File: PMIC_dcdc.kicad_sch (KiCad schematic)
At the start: 1 part, among them U3 RK809

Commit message: PMIC DCDC
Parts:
- added C10, C15, C16: 10uF X5R 6.3V, Resistor_SMD:R_0603_1608Metric, symbol Device:C
- added C11, C12, C13, C14, C17: 22uF X5R 6.3V, Resistor_SMD:R_0603_1608Metric, symbol Device:C
- added C18: 10uF 10V X5R, Capacitor_SMD:C_0201_0603Metric, symbol Device:C
- added C19: 10uF 10V X5R 10V, Capacitor_SMD:C_0201_0603Metric, symbol Device:C
- added C20: 22uF X5R 6.3V, Capacitor_SMD:C_0201_0603Metric, symbol Device:C
- added C9: 10uF 10V X5R, symbol Device:C
- added L1, L2, L3, L4: 470nH 0.035ohm, symbol Device:L
- added R11, R12: 100R 5%, Resistor_SMD:R_0402_1005Metric, symbol Device:R
- added R13: 110K 1%, Resistor_SMD:R_0402_1005Metric, symbol Device:R
- added R14: 120K 1%, Resistor_SMD:R_0402_1005Metric, symbol Device:R
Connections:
- net VCC5V0_SYS: now reaches U3.10 (VCC2)
- net VCC5V0_SYS: now also U3.11 (VCC1), U3.24 (VCC3), U3.66 (VCC4), C18.2, C19.2, C9.2
- net at U3.12 (SW1): now also L1.2
- net VDD_NPU_VEPU: now reaches U3.13 (FB1)
- net VDD_NPU_VEPU: now also C10.1, C11.1, C12.1, L1.1, R11.1, R11.2
- net at U3.25 (SW3): now also L3.2
- net VDD_DDR: now reaches U3.26 (VBUCK3)
- net VDD_DDR: now also C16.1, C17.1, L3.1, R13.1
- net at U3.27 (FB3): now also R13.2, R14.1
- net VCC_3V3: now reaches U3.64 (FB4)
- net VCC_3V3: now also C20.2, L4.1
- net at U3.65 (SW4): now also L4.2
- net VDD_ARM: now reaches U3.8 (FB2)
- net VDD_ARM: now also C13.1, C14.1, C15.1, L2.1, R12.1, R12.2
- net at U3.9 (SW2): now also L2.2
- new net GND: C10.2, C11.2, C12.2, C13.2, C14.2, C15.2, C16.2, C17.2, C18.1, C19.1, C20.1, C9.1, R14.2
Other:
- note added: "Feedback from far-end"
- company: (none) -> Qingdao IotPi Information Technology
- title: (none) -> Leaf RV1126 PMIC RK809
- moved on the sheet: U3C

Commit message: updated PMIC DCDC
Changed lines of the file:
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@@
+    (stroke (width 0) (type default))
+  )
+  (wire (pts (xy 54.61 43.18) (xy 67.31 43.18))
     (stroke (width 0) (type default))
   )
@@
     (effects (font (size 1.27 1.27)) (justify left bottom))
   )
+  (label "VCC_3V3" (at 67.31 43.18 0) (fields_autoplaced)
+    (effects (font (size 1.27 1.27)) (justify left bottom))
+  )
   (label "VCC5V0_SYS" (at 123.19 49.53 180) (fields_autoplaced)
     (effects (font (size 1.27 1.27)) (justify right bottom))
@@
     (effects (font (size 1.27 1.27)) (justify right bottom))
   )
-  (global_label "VDD_ARM" (shape input) (at 54.61 38.1 180) (fields_autoplaced)
+  (global_label "VDD_ARM" (shape output) (at 54.61 38.1 180) (fields_autoplaced)
     (effects (font (size 1.27 1.27)) (justify right))
     (property "Intersheetrefs" "${INTERSHEET_REFS}" (at 43.298 38.1 0)
@@
     )
   )
-  (global_label "VDD_DDR" (shape input) (at 54.61 33.02 180) (fields_autoplaced)
+  (global_label "VDD_DDR" (shape output) (at 54.61 33.02 180) (fields_autoplaced)
     (effects (font (size 1.27 1.27)) (justify right))
     (property "Intersheetrefs" "${INTERSHEET_REFS}" (at 43.298 33.02 0)
@@
     )
   )
-  (global_label "VDD_NPU_VEPU" (shape input) (at 54.61 27.94 180) (fields_autoplaced)
+  (global_label "VCC_3V3" (shape output) (at 54.61 43.18 180) (fields_autoplaced)
+    (effects (font (size 1.27 1.27)) (justify right))
+    (property "Intersheetrefs" "${INTERSHEET_REFS}" (at 43.6004 43.18 0)
+      (effects (font (size 1.27 1.27)) (justify right) hide)
+    )
+  )
+  (global_label "VDD_NPU_VEPU" (shape output) (at 54.61 27.94 180) (fields_autoplaced)
     (effects (font (size 1.27 1.27)) (justify right))
     (property "Intersheetrefs" "${INTERSHEET_REFS}" (at 37.3713 27.94 0)

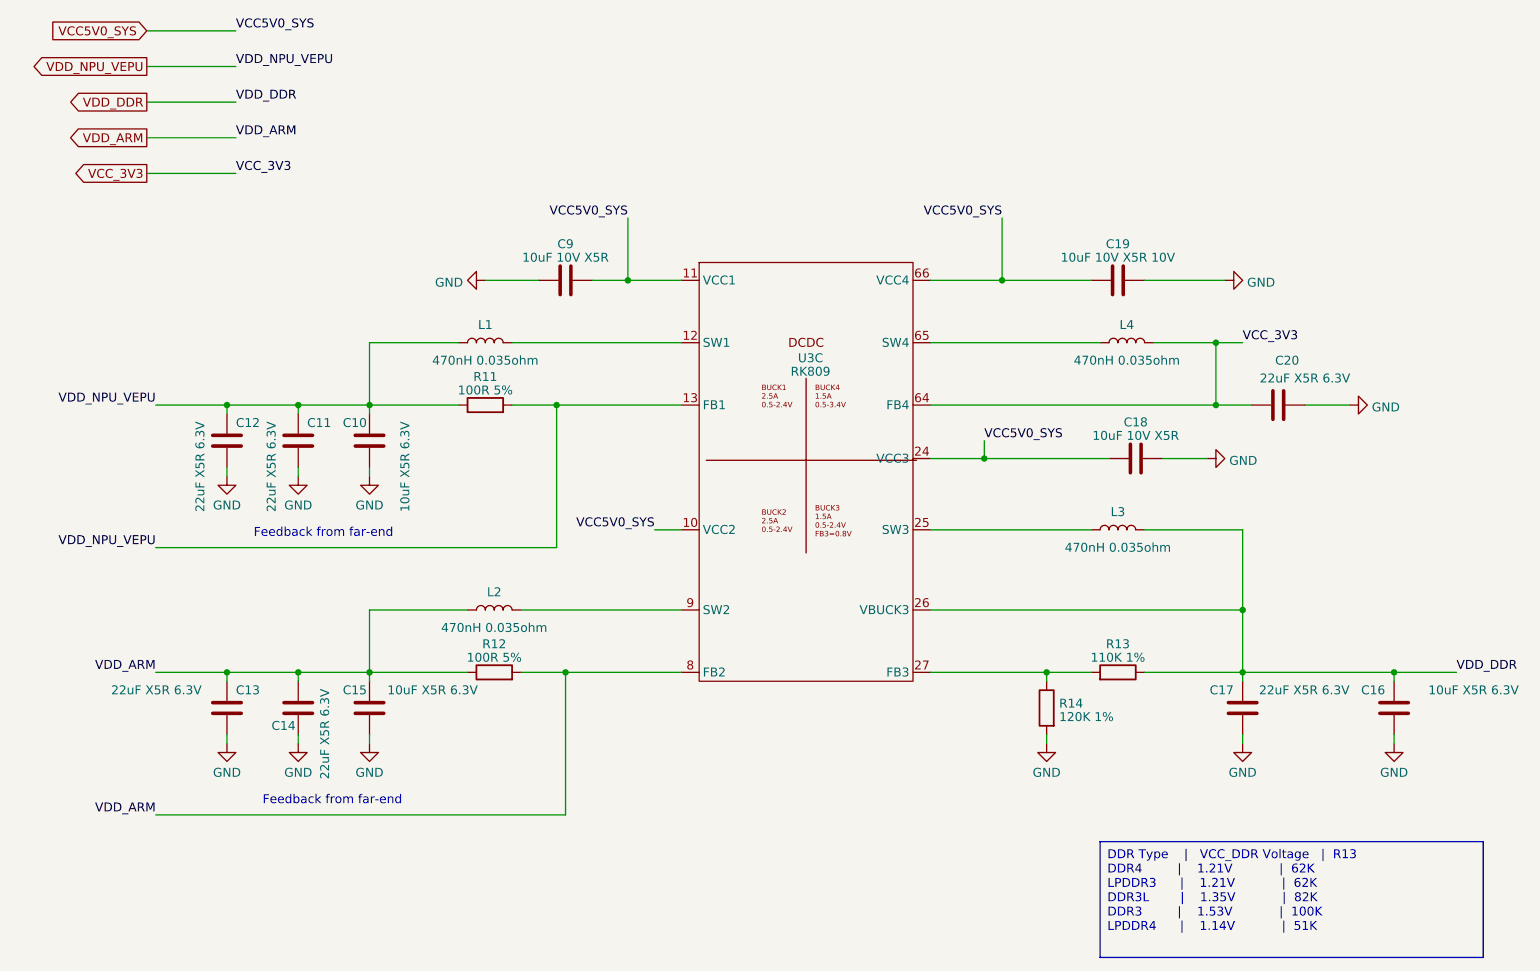
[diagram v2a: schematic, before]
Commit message: PMIC LDO
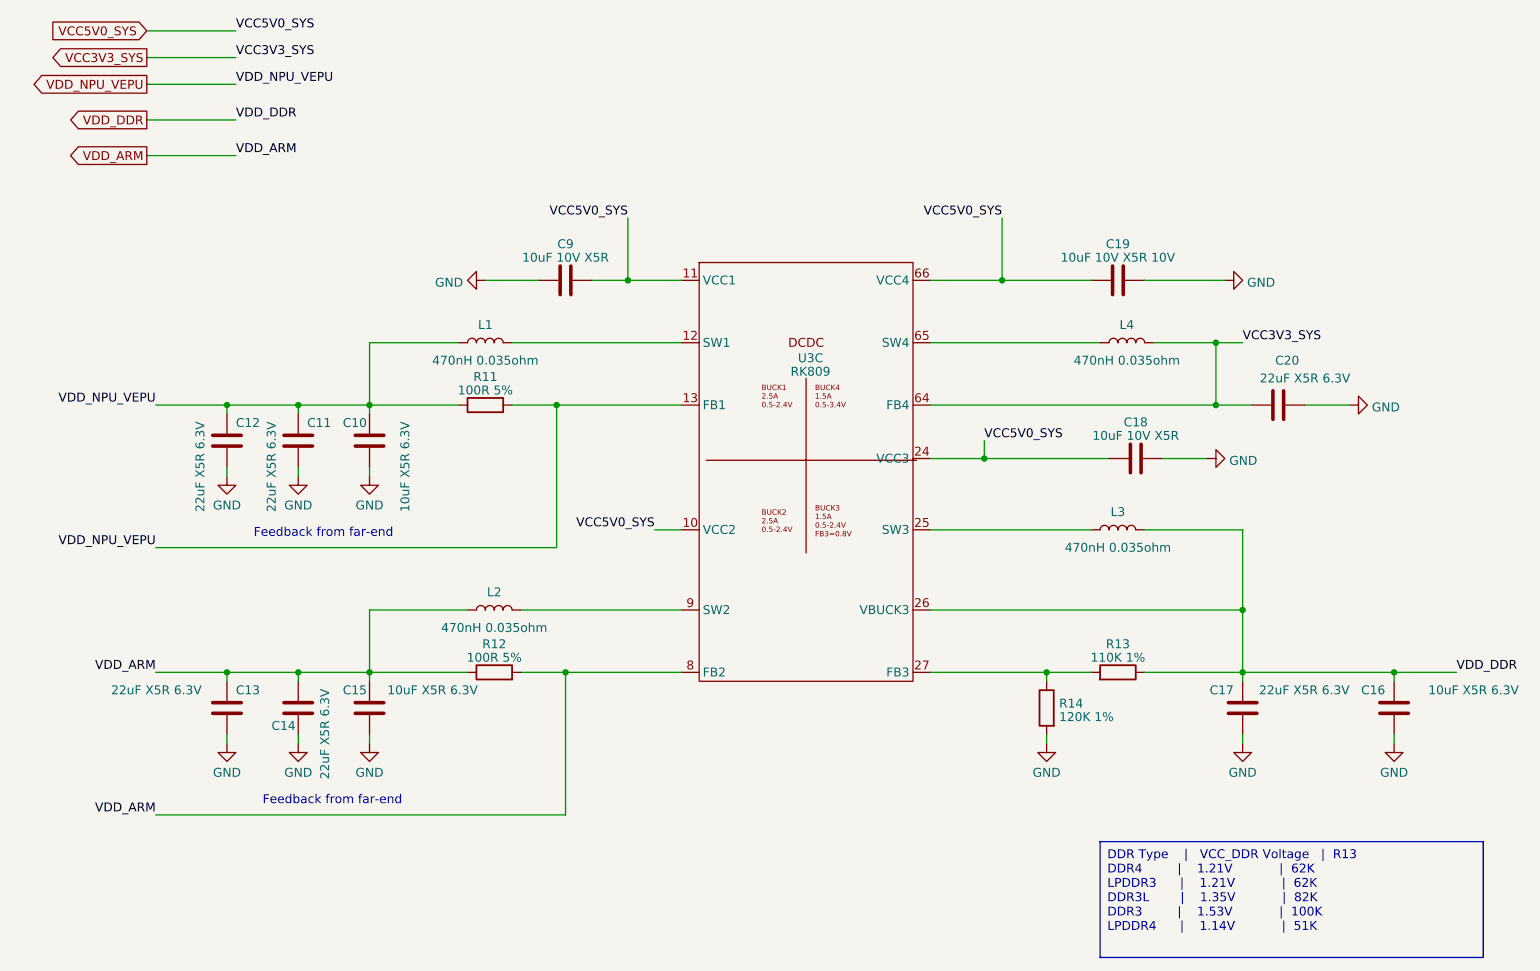
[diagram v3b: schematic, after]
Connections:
- net VCC_3V3 renamed VCC3V3_SYS
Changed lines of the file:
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@@
     (stroke (width 0) (type default))
   )
-  (wire (pts (xy 54.61 33.02) (xy 67.31 33.02))
+  (wire (pts (xy 54.61 35.56) (xy 67.31 35.56))
     (stroke (width 0) (type default))
   )
@@
     (stroke (width 0) (type default))
   )
-  (wire (pts (xy 54.61 38.1) (xy 67.31 38.1))
+  (wire (pts (xy 54.61 40.64) (xy 67.31 40.64))
     (stroke (width 0) (type default))
   )
@@
     (stroke (width 0) (type default))
   )
-  (wire (pts (xy 54.61 43.18) (xy 67.31 43.18))
+  (wire (pts (xy 54.61 26.67) (xy 67.31 26.67))
     (stroke (width 0) (type default))
   )
@@
     (stroke (width 0) (type default))
   )
-  (wire (pts (xy 54.61 27.94) (xy 67.31 27.94))
+  (wire (pts (xy 54.61 30.48) (xy 67.31 30.48))
     (stroke (width 0) (type default))
   )
@@
     (effects (font (size 1.27 1.27) (color 221 133 0 1)) (justify left bottom))
   )
-  (label "VDD_DDR" (at 67.31 33.02 0) (fields_autoplaced)
+  (label "VDD_DDR" (at 67.31 35.56 0) (fields_autoplaced)
     (effects (font (size 1.27 1.27)) (justify left bottom))
   )
@@
     (effects (font (size 1.27 1.27)) (justify left bottom))
   )
-  (label "VCC_3V3" (at 67.31 43.18 0) (fields_autoplaced)
+  (label "VCC3V3_SYS" (at 67.31 26.67 0) (fields_autoplaced)
     (effects (font (size 1.27 1.27)) (justify left bottom))
   )
@@
     (effects (font (size 1.27 1.27)) (justify right bottom))
   )
-  (label "VDD_NPU_VEPU" (at 67.31 27.94 0) (fields_autoplaced)
-    (effects (font (size 1.27 1.27)) (justify left bottom))
-  )
-  (label "VCC_3V3" (at 210.82 67.31 0) (fields_autoplaced)
+  (label "VDD_NPU_VEPU" (at 67.31 30.48 0) (fields_autoplaced)
+    (effects (font (size 1.27 1.27)) (justify left bottom))
+  )
+  (label "VCC3V3_SYS" (at 210.82 67.31 0) (fields_autoplaced)
     (effects (font (size 1.27 1.27)) (justify left bottom))
   )
@@
     (effects (font (size 1.27 1.27)) (justify right bottom))
   )
-  (label "VDD_ARM" (at 67.31 38.1 0) (fields_autoplaced)
+  (label "VDD_ARM" (at 67.31 40.64 0) (fields_autoplaced)
     (effects (font (size 1.27 1.27)) (justify left bottom))
   )
@@
     (effects (font (size 1.27 1.27)) (justify right bottom))
   )
-  (global_label "VDD_ARM" (shape output) (at 54.61 38.1 180) (fields_autoplaced)
-    (effects (font (size 1.27 1.27)) (justify right))
-    (property "Intersheetrefs" "${INTERSHEET_REFS}" (at 43.298 38.1 0)
+  (global_label "VDD_ARM" (shape output) (at 54.61 40.64 180) (fields_autoplaced)
+    (effects (font (size 1.27 1.27)) (justify right))
+    (property "Intersheetrefs" "${INTERSHEET_REFS}" (at 43.298 40.64 0)
       (effects (font (size 1.27 1.27)) (justify right) hide)
     )
@@
     )
   )
-  (global_label "VDD_DDR" (shape output) (at 54.61 33.02 180) (fields_autoplaced)
-    (effects (font (size 1.27 1.27)) (justify right))
-    (property "Intersheetrefs" "${INTERSHEET_REFS}" (at 43.298 33.02 0)
-      (effects (font (size 1.27 1.27)) (justify right) hide)
-    )
-  )
-  (global_label "VCC_3V3" (shape output) (at 54.61 43.18 180) (fields_autoplaced)
-    (effects (font (size 1.27 1.27)) (justify right))
-    (property "Intersheetrefs" "${INTERSHEET_REFS}" (at 43.6004 43.18 0)
-      (effects (font (size 1.27 1.27)) (justify right) hide)
-    )
-  )
-  (global_label "VDD_NPU_VEPU" (shape output) (at 54.61 27.94 180) (fields_autoplaced)
-    (effects (font (size 1.27 1.27)) (justify right))
-    (property "Intersheetrefs" "${INTERSHEET_REFS}" (at 37.3713 27.94 0)
-      (effects (font (size 1.27 1.27)) (justify right) hide)
-    )
+  (global_label "VDD_DDR" (shape output) (at 54.61 35.56 180) (fields_autoplaced)
+    (effects (font (size 1.27 1.27)) (justify right))
+    (property "Intersheetrefs" "${INTERSHEET_REFS}" (at 43.298 35.56 0)
+      (effects (font (size 1.27 1.27)) (justify right) hide)
+    )
+  )
+  (global_label "VCC3V3_SYS" (shape output) (at 54.61 26.67 180) (fields_autoplaced)
+    (effects (font (size 1.27 1.27)) (justify right))
+    (property "Intersheetrefs" "${INTERSHEET_REFS}" (at 40.0928 26.67 0)
+      (effects (font (size 1.27 1.27)) (justify right) hide)
+    )
+  )
+  (global_label "VDD_NPU_VEPU" (shape output) (at 54.61 30.48 180) (fields_autoplaced)
+    (effects (font (size 1.27 1.27)) (justify right))
+    (property "Intersheetrefs" "${INTERSHEET_REFS}" (at 37.3713 30.48 0)
+      (effects (font (size 1.27 1.27)) (justify right) hide)
+    )

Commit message: updated: PMIC codec
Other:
- title: Leaf RV1126 PMIC RK809 -> Leaf RV1126 PMIC RK809 Codec
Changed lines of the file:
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@@
   (paper "A4")
   (title_block
-    (title "Leaf RV1126 PMIC RK809")
-    (date "2023-02-23")
+    (title "Leaf RV1126 PMIC RK809 Codec")
+    (date "2023-02-25")
     (rev "1")
     (company "Qingdao IotPi Information Technology")

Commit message: updated: titles
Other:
- title: Leaf RV1126 PMIC RK809 Codec -> Leaf RV1126 RK809 DCDC
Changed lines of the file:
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@@
   (paper "A4")
   (title_block
-    (title "Leaf RV1126 PMIC RK809 Codec")
+    (title "Leaf RV1126 RK809 DCDC")
     (date "2023-02-25")
     (rev "1")

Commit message: Updated eMMC
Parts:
- U3: value RK809 -> RK809-2
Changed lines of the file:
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@@
       (effects (font (size 1.27 1.27)))
     )
-    (property "Value" "RK809" (at 149.225 71.4281 0)
+    (property "Value" "RK809-2" (at 149.225 71.4281 0)
       (effects (font (size 1.27 1.27)))
     )

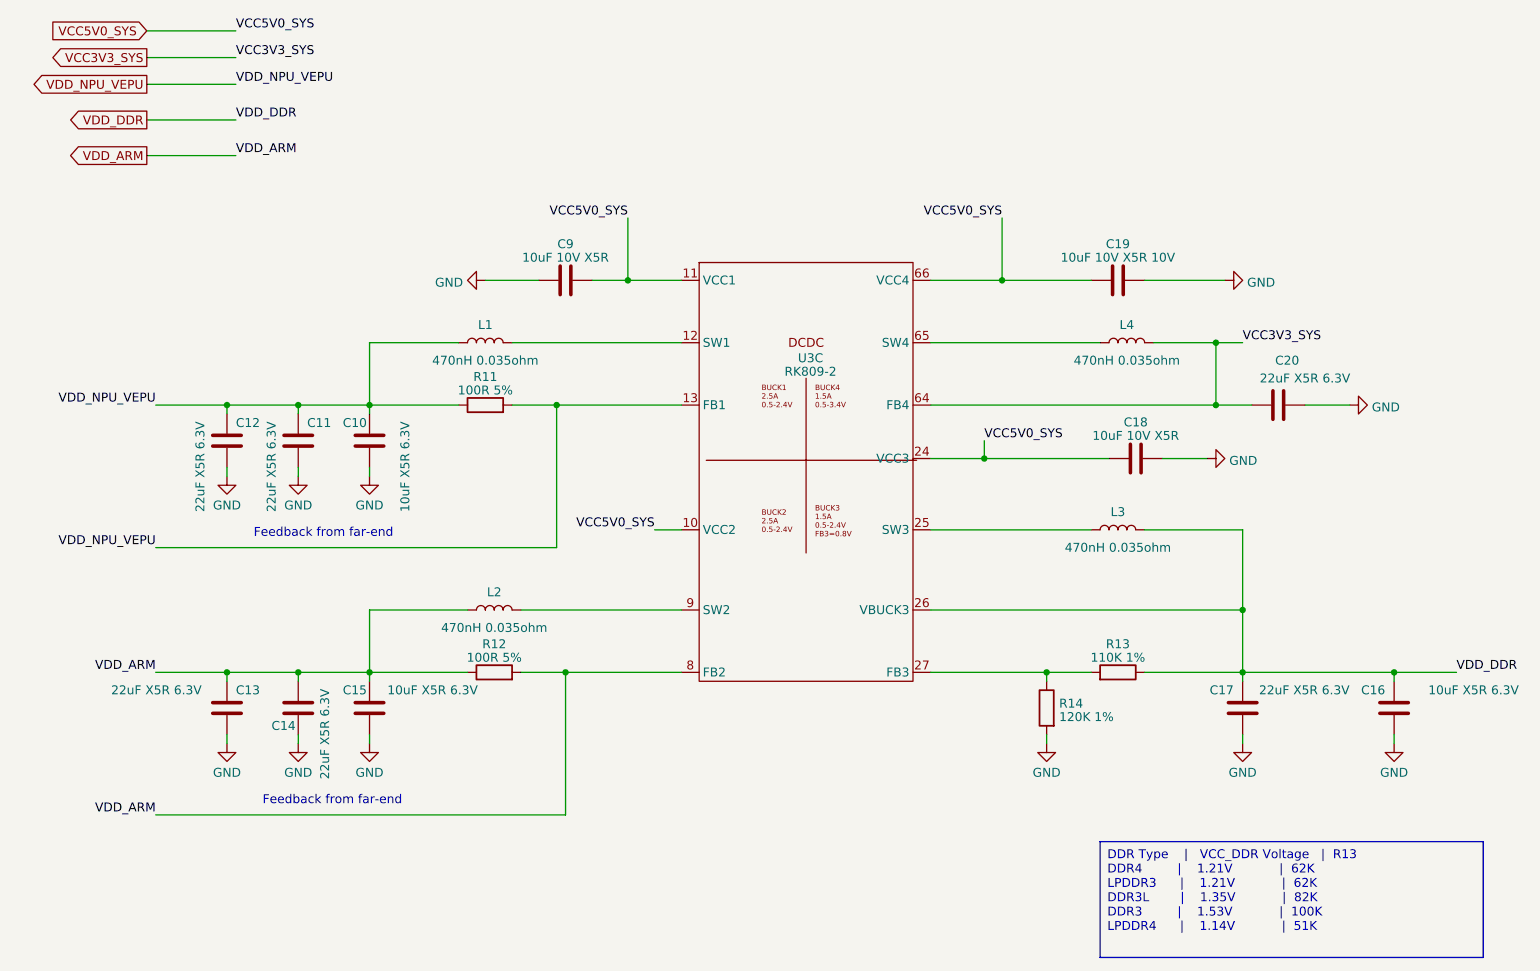
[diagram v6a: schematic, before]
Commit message: updated footprints
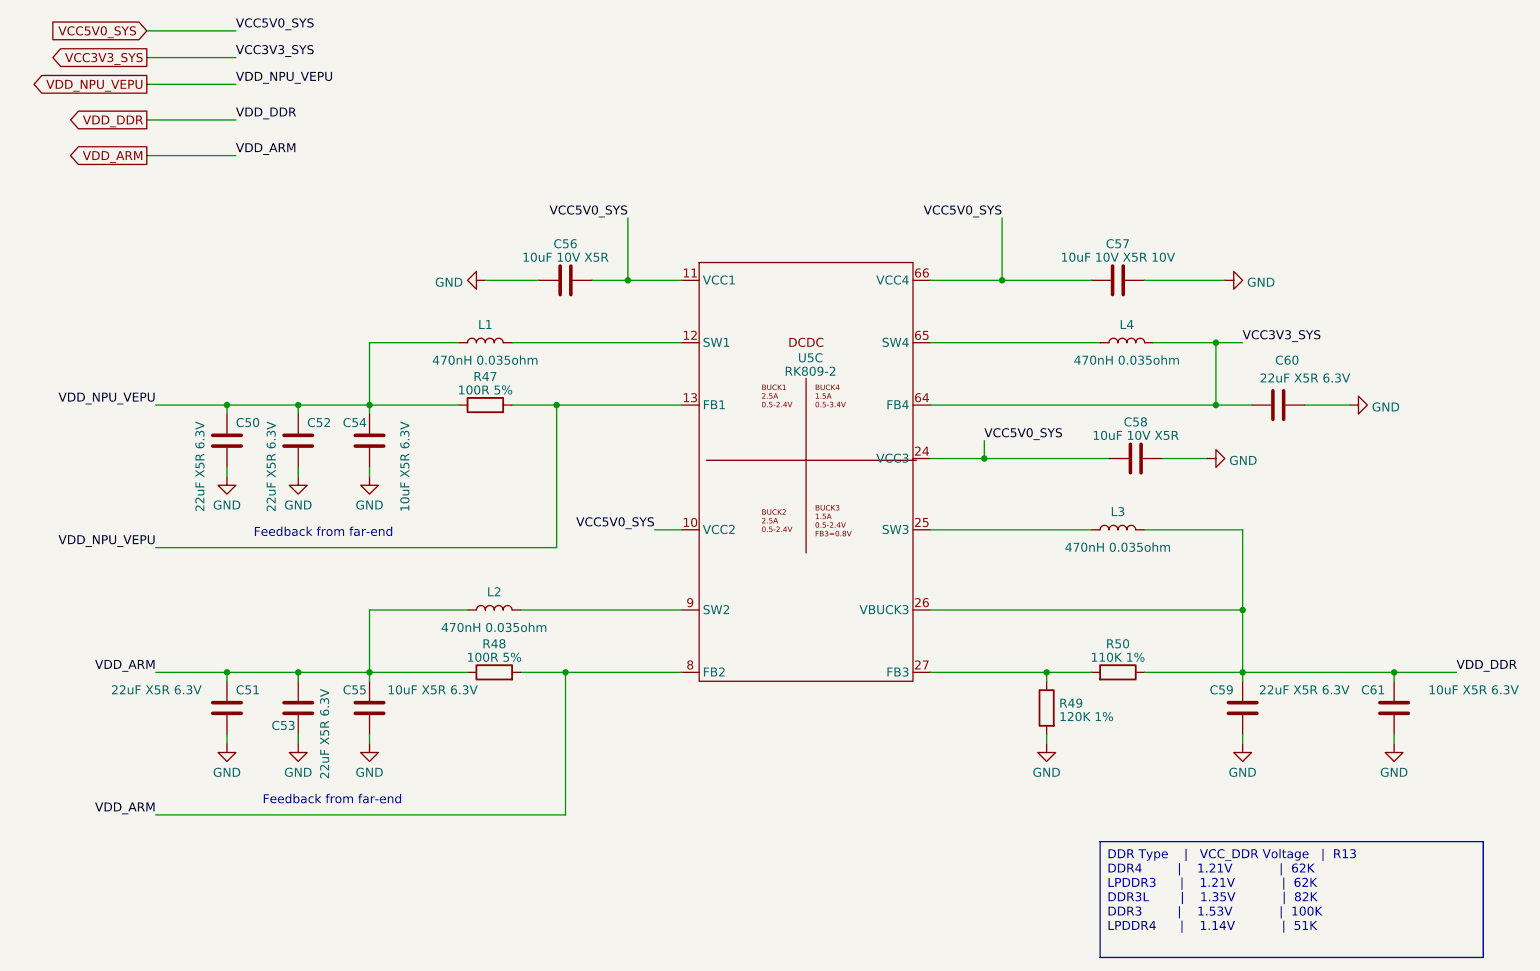
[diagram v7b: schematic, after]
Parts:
- renumbered C12 to C50, C13 to C51, C11 to C52, C14 to C53, C10 to C54, C15 to C55, C9 to C56, C19 to C57, C18 to C58, C17 to C59, C20 to C60, C16 to C61, R11 to R47, R12 to R48, R14 to R49, R13 to R50, U3 to U5
